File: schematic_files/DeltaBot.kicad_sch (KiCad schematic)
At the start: 17 parts, among them J1 USB C PD Modulle, J2 LIDAR, J3 MOTOR_L, J4 MOTOR_R, SW1 SW_SPDT, U1 Radxa_ROCK5B, U2 Buck Converter

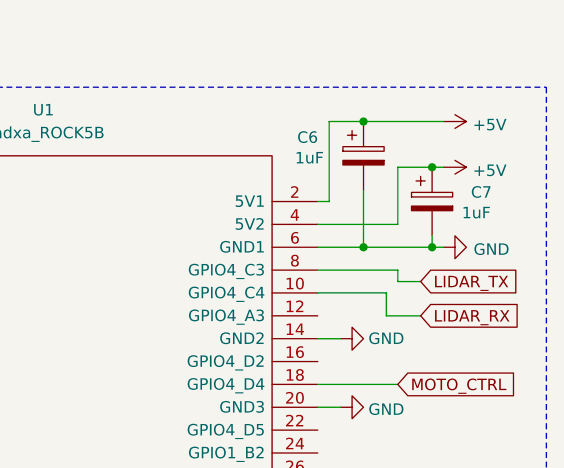
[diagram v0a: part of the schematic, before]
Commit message: Schematic minor fixes
rearranged silkscreen, added capacitors to the pcb
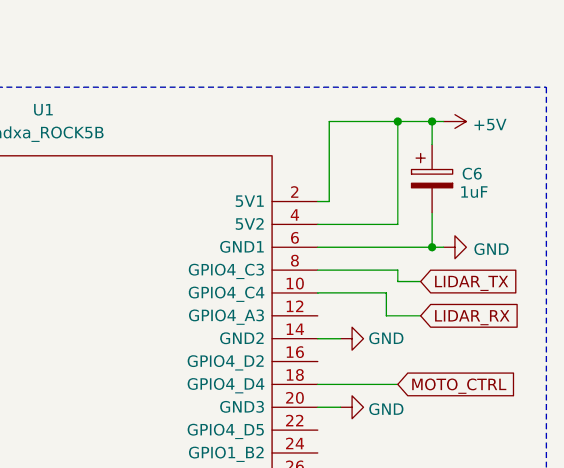
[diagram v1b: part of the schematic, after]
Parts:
- removed C7: 1uF, symbol Device:C_Polarized
- C1: footprint (none) -> deltabot:CP_Radial_D12.5mm_P5.00mm
- C2, C3, C4, C5, C6: footprint (none) -> deltabot:C_Disc_D3.0mm_W2.0mm_P2.50mm
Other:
- moved on the sheet: C6
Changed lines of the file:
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@@
 	)
 	(junction
-		(at 172.72 40.64)
-		(diameter 0)
-		(color 0 0 0 0)
-	)
-	(junction
 		(at 66.04 102.87)
 		(diameter 0)
@@
 	)
 	(junction
-		(at 172.72 26.67)
-		(diameter 0)
-		(color 0 0 0 0)
-	)
-	(junction
 		(at 63.5 95.25)
 		(diameter 0)
@@
 	)
 	(junction
-		(at 180.34 31.75)
+		(at 180.34 26.67)
 		(diameter 0)
 		(color 0 0 0 0)
@@
 	)
 	(junction
+		(at 176.53 26.67)
+		(diameter 0)
+		(color 0 0 0 0)
+	)
+	(junction
 		(at 24.13 110.49)
 		(diameter 0)
@@
 	(wire
 		(pts
-			(xy 180.34 39.37) (xy 180.34 40.64)
+			(xy 180.34 36.83) (xy 180.34 40.64)
 		)
 		(stroke
@@
 	(wire
 		(pts
-			(xy 172.72 26.67) (xy 181.61 26.67)
-		)
-		(stroke
-			(width 0)
-			(type default)
-		)
-	)
-	(wire
-		(pts
 			(xy 66.04 64.77) (xy 76.2 64.77)
 		)
@@
 	(wire
 		(pts
-			(xy 180.34 31.75) (xy 181.61 31.75)
-		)
-		(stroke
-			(width 0)
-			(type default)
-		)
-	)
-	(wire
-		(pts
 			(xy 40.64 119.38) (xy 40.64 118.11)
 		)
@@
 	(wire
 		(pts
-			(xy 167.64 40.64) (xy 172.72 40.64)
+			(xy 167.64 40.64) (xy 180.34 40.64)
 		)
 		(stroke
@@
 	(wire
 		(pts
-			(xy 176.53 31.75) (xy 176.53 38.1)
+			(xy 52.07 72.39) (xy 66.04 72.39)
 		)
 		(stroke
@@
 	(wire
 		(pts
-			(xy 52.07 72.39) (xy 66.04 72.39)
+			(xy 39.37 113.03) (xy 41.91 113.03)
 		)
 		(stroke
@@
 	(wire
 		(pts
-			(xy 172.72 40.64) (xy 180.34 40.64)
+			(xy 22.86 64.77) (xy 25.4 64.77)
 		)
 		(stroke
@@
 	(wire
 		(pts
-			(xy 39.37 113.03) (xy 41.91 113.03)
+			(xy 59.69 95.25) (xy 63.5 95.25)
 		)
 		(stroke
@@
 	(wire
 		(pts
-			(xy 22.86 64.77) (xy 25.4 64.77)
+			(xy 59.69 119.38) (xy 63.5 119.38)
 		)
 		(stroke
@@
 	(wire
 		(pts
-			(xy 59.69 95.25) (xy 63.5 95.25)
+			(xy 33.02 102.87) (xy 31.75 102.87)
 		)
 		(stroke
@@
 	(wire
 		(pts
-			(xy 59.69 119.38) (xy 63.5 119.38)
+			(xy 63.5 119.38) (xy 69.85 119.38)
 		)
 		(stroke
@@
 	(wire
 		(pts
-			(xy 33.02 102.87) (xy 31.75 102.87)
+			(xy 180.34 29.21) (xy 180.34 26.67)
 		)
 		(stroke
@@
 	(wire
 		(pts
-			(xy 63.5 119.38) (xy 69.85 119.38)
+			(xy 63.5 102.87) (xy 66.04 102.87)
 		)
 		(stroke
@@
 	(wire
 		(pts
-			(xy 172.72 34.29) (xy 172.72 40.64)
+			(xy 52.07 64.77) (xy 66.04 64.77)
 		)
 		(stroke
@@
 	(wire
 		(pts
-			(xy 63.5 102.87) (xy 66.04 102.87)
+			(xy 175.26 48.26) (xy 179.07 48.26)
 		)
 		(stroke
@@
 	(wire
 		(pts
-			(xy 52.07 64.77) (xy 66.04 64.77)
+			(xy 176.53 26.67) (xy 176.53 38.1)
 		)
 		(stroke
@@
 	(wire
 		(pts
-			(xy 175.26 48.26) (xy 179.07 48.26)
+			(xy 176.53 26.67) (xy 180.34 26.67)
 		)
 		(stroke
@@
 	(wire
 		(pts
+			(xy 180.34 26.67) (xy 181.61 26.67)
+		)
+		(stroke
+			(width 0)
+			(type default)
+		)
+	)
+	(wire
+		(pts
 			(xy 176.53 38.1) (xy 167.64 38.1)
 		)
@@
 	(wire
 		(pts
-			(xy 168.91 26.67) (xy 172.72 26.67)
+			(xy 168.91 26.67) (xy 176.53 26.67)
 		)
 		(stroke
@@
 	(wire
 		(pts
-			(xy 176.53 31.75) (xy 180.34 31.75)
-		)
-		(stroke
-			(width 0)
-			(type default)
-		)
-	)
-	(wire
-		(pts
 			(xy 168.91 35.56) (xy 167.64 35.56)
 		)
@@
 	(symbol
 		(lib_id "Device:C_Polarized")
-		(at 172.72 30.48 0)
+		(at 180.34 33.02 0)
 		(unit 1)
 		(exclude_from_sim no)
@@
 		(dnp no)
 		(property "Reference" "C6"
-			(at 165.354 28.448 0)
+			(at 183.642 32.512 0)
 			(effects
 				(font
@@
 		)
 		(property "Value" "1uF"
-			(at 165.1 30.734 0)
+			(at 183.388 34.544 0)
 			(effects
 				(font
@@
 			)
 		)
-		(property "Footprint" ""
-			(at 173.6852 34.29 0)
+		(property "Footprint" "deltabot:C_Disc_D3.0mm_W2.0mm_P2.50mm"
+			(at 181.3052 36.83 0)
 			(effects
 				(font
@@
 		)
 		(property "Datasheet" "~"
-			(at 172.72 30.48 0)
+			(at 180.34 33.02 0)
 			(effects
 				(font
@@
 		)
 		(property "Description" "Polarized capacitor"
-			(at 172.72 30.48 0)
+			(at 180.34 33.02 0)
 			(effects
 				(font
@@
 			)
 		)
-		(property "Footprint" ""
+		(property "Footprint" "deltabot:C_Disc_D3.0mm_W2.0mm_P2.50mm"
 			(at 64.4652 127 0)
 			(effects
@@
 			)
 		)
-		(property "Footprint" ""
+		(property "Footprint" "deltabot:C_Disc_D3.0mm_W2.0mm_P2.50mm"
 			(at 67.0052 72.39 0)
 			(effects
@@
 			)
 		)
-		(property "Footprint" ""
+		(property "Footprint" "deltabot:C_Disc_D3.0mm_W2.0mm_P2.50mm"
 			(at 64.4652 102.87 0)
 			(effects
@@
 	)
 	(symbol
-		(lib_id "power:+5V")
-		(at 181.61 31.75 270)
-		(unit 1)
-		(exclude_from_sim no)
-		(in_bom yes)
-		(on_board yes)
-		(dnp no)
-		(property "Reference" "#PWR026"
-			(at 177.8 31.75 0)
-			(effects
-				(font
-					(size 1.27 1.27)
-				)
-				(hide yes)
-			)
-		)
-		(property "Value" "+5V"
-			(at 184.8612 32.131 90)
-			(effects
-				(font
-					(size 1.27 1.27)
-				)
-				(justify left)
-			)
-		)
-		(property "Footprint" ""
-			(at 181.61 31.75 0)
-			(effects
-				(font
-					(size 1.27 1.27)
-				)
-				(hide yes)
-			)
-		)
-		(property "Datasheet" ""
-			(at 181.61 31.75 0)
-			(effects
-				(font
-					(size 1.27 1.27)
-				)
-				(hide yes)
-			)
-		)
-		(property "Description" ""
-			(at 181.61 31.75 0)
-			(effects
-				(font
-					(size 1.27 1.27)
-				)
-				(hide yes)
-			)
-		)
-		(pin "1"
-		)
-		(instances
-			(project "sigmabot"
-				(path "/9f04e495-2040-4ae6-9603-65340a735169"
-					(reference "#PWR026")
-					(unit 1)
-				)
-			)
-		)
-	)
-	(symbol
-		(lib_id "Device:C_Polarized")
-		(at 180.34 35.56 0)
-		(unit 1)
-		(exclude_from_sim no)
-		(in_bom yes)
-		(on_board yes)
-		(dnp no)
-		(property "Reference" "C7"
-			(at 184.658 34.544 0)
-			(effects
-				(font
-					(size 1.27 1.27)
-				)
-				(justify left)
-			)
-		)
-		(property "Value" "1uF"
-			(at 183.642 36.83 0)
-			(effects
-				(font
-					(size 1.27 1.27)
-				)
-				(justify left)
-			)
-		)
-		(property "Footprint" ""
-			(at 181.3052 39.37 0)
-			(effects
-				(font
-					(size 1.27 1.27)
-				)
-				(hide yes)
-			)
-		)
-		(property "Datasheet" "~"
-			(at 180.34 35.56 0)
-			(effects
-				(font
-					(size 1.27 1.27)
-				)
-				(hide yes)
-			)
-		)
-		(property "Description" "Polarized capacitor"
-			(at 180.34 35.56 0)
-			(effects
-				(font
-					(size 1.27 1.27)
-				)
-				(hide yes)
-			)
-		)
-		(pin "2"
-		)
-		(pin "1"
-		)
-		(instances
-			(project "DeltaBot"
-				(path "/9f04e495-2040-4ae6-9603-65340a735169"
-					(reference "C7")
-					(unit 1)
-				)
-			)
-		)
-	)
-	(symbol
 		(lib_id "power:GND")
 		(at 170.18 76.2 90)
@@
 			)
 		)
-		(property "Footprint" ""
+		(property "Footprint" "deltabot:CP_Radial_D12.5mm_P5.00mm"
 			(at 53.0352 72.39 0)
 			(effects
@@
 			)
 		)
-		(property "Footprint" ""
+		(property "Footprint" "deltabot:C_Disc_D3.0mm_W2.0mm_P2.50mm"
 			(at 25.0952 119.38 0)
 			(effects

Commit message: adjusted labeling
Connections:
- net LIDAR_RX: now also U1.8 (GPIO4_C3); no longer U1.10 (GPIO4_C4)
- net LIDAR_TX: now also U1.10 (GPIO4_C4); no longer U1.8 (GPIO4_C3)
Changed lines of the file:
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@@
 		)
 	)
-	(global_label "LIDAR_TX"
+	(global_label "LIDAR_RX"
 		(shape input)
 		(at 179.07 44.45 0)
@@
 		)
 	)
-	(global_label "LIDAR_RX"
+	(global_label "LIDAR_TX"
 		(shape input)
 		(at 179.07 48.26 0)
